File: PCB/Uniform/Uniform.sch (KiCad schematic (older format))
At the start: 158 parts, among them J2 M50-3500542, U1 STM32F373CCT6, U2 TLV1117-33, X1 XTAL_GND

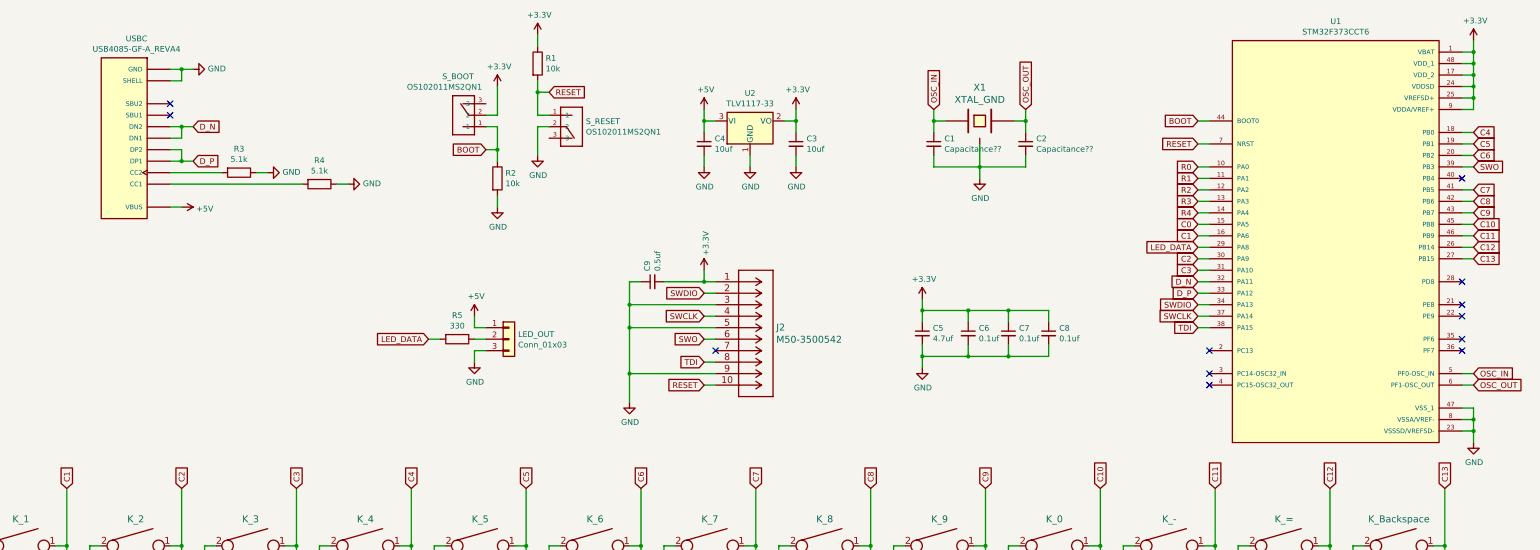
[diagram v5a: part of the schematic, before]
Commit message: Switched MCUs to STM32L072KZT6 because the F3 series went out of stock..
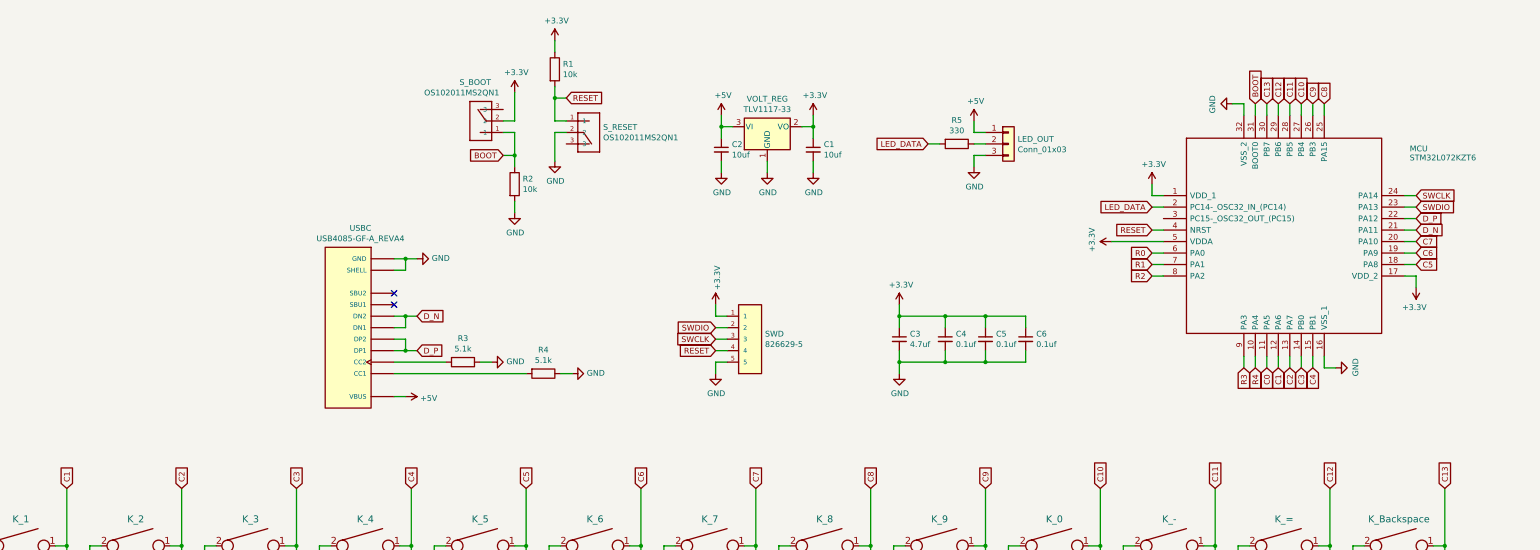
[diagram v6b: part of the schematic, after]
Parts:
- removed C1, C2: Capacitance??, symbol Device:C_Small
- removed C9: 0.5uf, symbol Device:C_Small
- removed J2: M50-3500542, CONN10_500542_HRW, symbol ul_M50-3500542:M50-3500542
- removed U1: STM32F373CCT6, QFP50P900X900X160-48N, symbol STM32F373CCT6:STM32F373CCT6
- removed X1: XTAL_GND, symbol keyboard_parts:XTAL_GND
- added MCU: STM32L072KZT6, QFP80P900X900X160-32N, symbol SamacSys_Parts:STM32L072KZT6
- added SWD: 826629-5, TE_826629-5, symbol 826629-5:826629-5
- renumbered C3 to C1, C4 to C2, C5 to C3, C6 to C4, C7 to C5, C8 to C6, U2 to VOLT_REG
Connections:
- net +3V3: now also MCU.1 (VDD_1), MCU.17 (VDD_2), MCU.5 (VDDA), SWD.1
- net BOOT: now also MCU.31 (BOOT0)
- net C0: now also MCU.11 (PA5)
- net C1: now also MCU.12 (PA6)
- net C10: now also MCU.27 (PB4)
- net C11: now also MCU.28 (PB5)
- net C12: now also MCU.29 (PB6)
- net C13: now also MCU.30 (PB7)
- net C2: now also MCU.13 (PA7)
- net C3: now also MCU.14 (PB0)
- net C4: now also MCU.15 (PB1)
- net C5: now also MCU.18 (PA8)
- net C6: now also MCU.19 (PA9)
- net C7: now also MCU.20 (PA10)
- net C8: now also MCU.25 (PA15)
- net C9: now also MCU.26 (PB3)
- net D_N: now also MCU.21 (PA11)
- net D_P: now also MCU.22 (PA12)
- net GND: now also MCU.16 (VSS_1), MCU.32 (VSS_2), SWD.5
- net LED_DATA: now also MCU.2 (PC14-_OSC32_IN_(PC14))
- net R0: now also MCU.6 (PA0)
- net R1: now also MCU.7 (PA1)
- net R2: now also MCU.8 (PA2)
- net R3: now also MCU.9 (PA3)
- net R4: now also MCU.10 (PA4)
- net RESET: now also MCU.4 (NRST), SWD.4
- net SWCLK: now also MCU.24 (PA14), SWD.3
- net SWDIO: now also MCU.23 (PA13), SWD.2
- no-connect marks 12 -> 2
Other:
- moved on the sheet: C1, C2, C3, C4, C5, C6, LED_OUT, R1, R2, R3, R4, R5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

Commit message: Schematic complete
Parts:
- removed C3: 4.7uf, symbol Device:C_Small
- removed MCU: STM32L072KZT6, QFP80P900X900X160-32N, symbol SamacSys_Parts:STM32L072KZT6
- added C6: 1uf, symbol Device:C_Small
- added MCU: STM32L072KZT6, QFP80P900X900X160-32N, symbol STM32L072KZT6:STM32L072KZT6
- added POWER_LED: LED, symbol Device:LED
- added R6: R, symbol Device:R
- renumbered C4 to C3, C6 to C4
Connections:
- net +3V3: now also C6.1, MCU.1 (VDD_1), MCU.17 (VDD_2), MCU.5 (VDDA)
- net BOOT: now also MCU.31 (BOOT0)
- net C0: now also MCU.11 (PA5)
- net C1: now also MCU.12 (PA6)
- net C10: now also MCU.27 (PB4)
- net C11: now also MCU.28 (PB5)
- net C12: now also MCU.29 (PB6)
- net C13: now also MCU.30 (PB7)
- net C2: now also MCU.13 (PA7)
- net C3: now also MCU.14 (PB0)
- net C4: now also MCU.15 (PB1)
- net C5: now also MCU.18 (PA8)
- net C6: now also MCU.19 (PA9)
- net C7: now also MCU.20 (PA10)
- net C8: now also MCU.25 (PA15)
- net C9: now also MCU.26 (PB3)
- net D_N: now also MCU.21 (PA11)
- net D_P: now also MCU.22 (PA12)
- net GND: now also C6.2, MCU.16 (VSS_1), MCU.32 (VSS_2), POWER_LED.1 (K)
- net LED_DATA: now also MCU.2 (PC14-_OSC32_IN_(PC14))
- net R0: now also MCU.6 (PA0)
- net R1: now also MCU.7 (PA1)
- net R2: now also MCU.8 (PA2)
- net R3: now also MCU.9 (PA3)
- net R4: now also MCU.10 (PA4)
- net RESET: now also MCU.4 (NRST)
- net SWCLK: now also MCU.24 (PA14)
- net SWDIO: now also MCU.23 (PA13)
- new net: POWER_LED.2 (A), R6.2
- new net STATUS_LED_DATA: MCU.3 (PC15-_OSC32_OUT_(PC15)), R6.1
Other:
- moved on the sheet: C3, C4, LED_OUT, R3, R4, R5, SWD, USBC

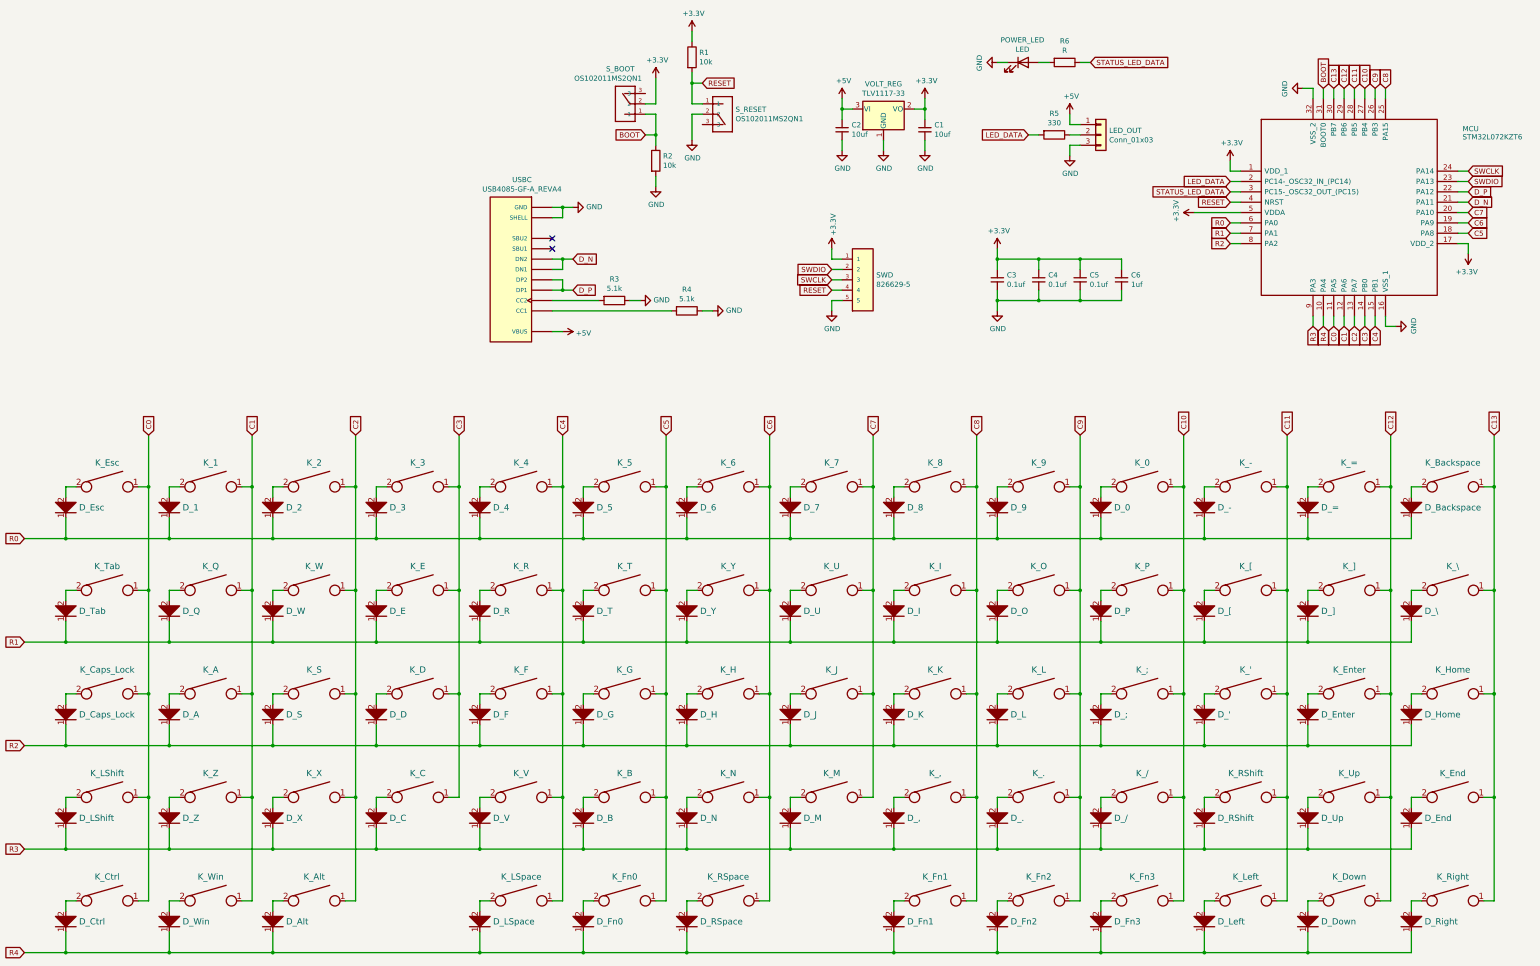
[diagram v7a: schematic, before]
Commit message: switch footprints layed out on PCB
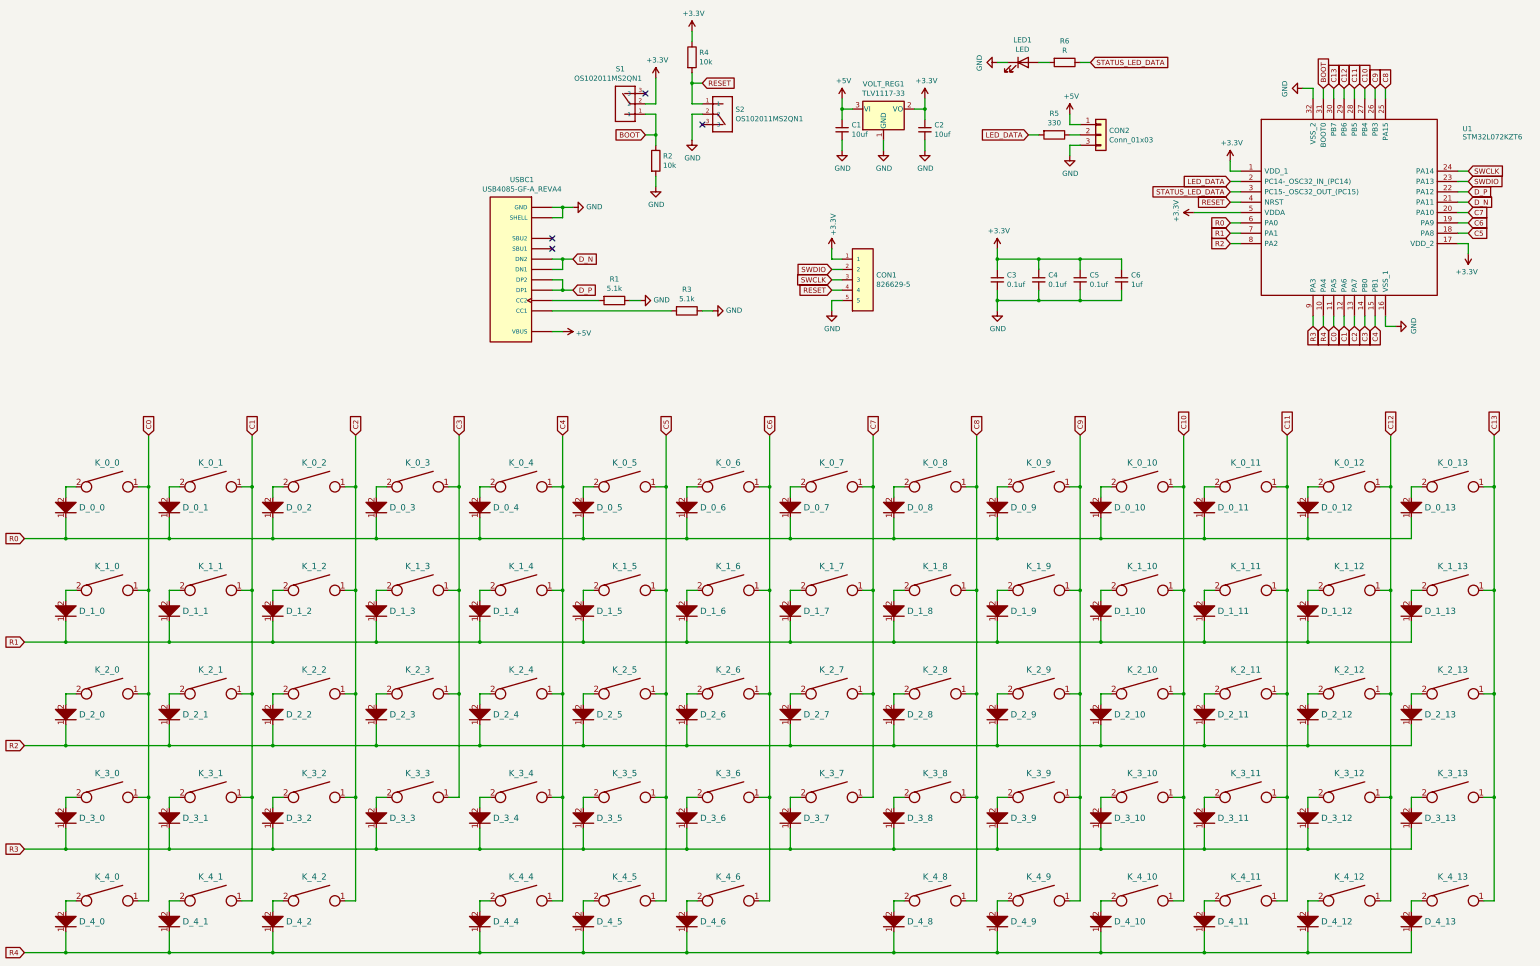
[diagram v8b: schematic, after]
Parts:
- C1: renamed from C2; footprint (none) -> ul_FG16X7R1E106KRT06:FG16X7R1E106KRT06
- C2: renamed from C1; footprint (none) -> ul_FG16X7R1E106KRT06:FG16X7R1E106KRT06
- C3, C4, C5: footprint (none) -> Resistor_THT:R_Axial_DIN0207_L6.3mm_D2.5mm_P7.62mm_Horizontal
- C6: footprint (none) -> RDER71H105K2M1H03A:CAP_RDER71H105K2M1H03A
- CON1: renamed from SWD; footprint TE_826629-5 -> 826629-5:TE_826629-5
- CON2: renamed from LED_OUT; footprint (none) -> Connector_PinHeader_2.54mm:PinHeader_1x03_P2.54mm_Vertical
- D_0_0: renamed from D_Esc; footprint (none) -> 1N4148:DIOAD829W49L456D191
- D_0_1: renamed from D_1; footprint (none) -> 1N4148:DIOAD829W49L456D191
- D_0_10: renamed from D_0; footprint (none) -> 1N4148:DIOAD829W49L456D191
- D_0_11: renamed from D_-; footprint (none) -> 1N4148:DIOAD829W49L456D191
- D_0_12: renamed from D_=; footprint (none) -> 1N4148:DIOAD829W49L456D191
- D_0_13: renamed from D_Backspace; footprint (none) -> 1N4148:DIOAD829W49L456D191
- D_0_2: renamed from D_2; footprint (none) -> 1N4148:DIOAD829W49L456D191
- D_0_3: renamed from D_3; footprint (none) -> 1N4148:DIOAD829W49L456D191
- D_0_4: renamed from D_4; footprint (none) -> 1N4148:DIOAD829W49L456D191
- D_0_5: renamed from D_5; footprint (none) -> 1N4148:DIOAD829W49L456D191
- D_0_6: renamed from D_6; footprint (none) -> 1N4148:DIOAD829W49L456D191
- D_0_7: renamed from D_7; footprint (none) -> 1N4148:DIOAD829W49L456D191
- D_0_8: renamed from D_8; footprint (none) -> 1N4148:DIOAD829W49L456D191
- D_0_9: renamed from D_9; footprint (none) -> 1N4148:DIOAD829W49L456D191
- D_1_0: renamed from D_Tab; footprint (none) -> 1N4148:DIOAD829W49L456D191
- D_1_1: renamed from D_Q; footprint (none) -> 1N4148:DIOAD829W49L456D191
- D_1_10: renamed from D_P; footprint (none) -> 1N4148:DIOAD829W49L456D191
- D_1_11: renamed from D_[; footprint (none) -> 1N4148:DIOAD829W49L456D191
- D_1_12: renamed from D_]; footprint (none) -> 1N4148:DIOAD829W49L456D191
- D_1_13: renamed from D_\; footprint (none) -> 1N4148:DIOAD829W49L456D191
- D_1_2: renamed from D_W; footprint (none) -> 1N4148:DIOAD829W49L456D191
- D_1_3: renamed from D_E; footprint (none) -> 1N4148:DIOAD829W49L456D191
- D_1_4: renamed from D_R; footprint (none) -> 1N4148:DIOAD829W49L456D191
- D_1_5: renamed from D_T; footprint (none) -> 1N4148:DIOAD829W49L456D191
- D_1_6: renamed from D_Y; footprint (none) -> 1N4148:DIOAD829W49L456D191
- D_1_7: renamed from D_U; footprint (none) -> 1N4148:DIOAD829W49L456D191
- D_1_8: renamed from D_I; footprint (none) -> 1N4148:DIOAD829W49L456D191
- D_1_9: renamed from D_O; footprint (none) -> 1N4148:DIOAD829W49L456D191
- D_2_0: renamed from D_Caps_Lock; footprint (none) -> 1N4148:DIOAD829W49L456D191
- D_2_1: renamed from D_A; footprint (none) -> 1N4148:DIOAD829W49L456D191
- D_2_10: renamed from D_;; footprint (none) -> 1N4148:DIOAD829W49L456D191
- D_2_11: renamed from D_'; footprint (none) -> 1N4148:DIOAD829W49L456D191
- D_2_12: renamed from D_Enter; footprint (none) -> 1N4148:DIOAD829W49L456D191
- D_2_13: renamed from D_Home; footprint (none) -> 1N4148:DIOAD829W49L456D191
- D_2_2: renamed from D_S; footprint (none) -> 1N4148:DIOAD829W49L456D191
- D_2_3: renamed from D_D; footprint (none) -> 1N4148:DIOAD829W49L456D191
- D_2_4: renamed from D_F; footprint (none) -> 1N4148:DIOAD829W49L456D191
- D_2_5: renamed from D_G; footprint (none) -> 1N4148:DIOAD829W49L456D191
- D_2_6: renamed from D_H; footprint (none) -> 1N4148:DIOAD829W49L456D191
- D_2_7: renamed from D_J; footprint (none) -> 1N4148:DIOAD829W49L456D191
- D_2_8: renamed from D_K; footprint (none) -> 1N4148:DIOAD829W49L456D191
- D_2_9: renamed from D_L; footprint (none) -> 1N4148:DIOAD829W49L456D191
- D_3_0: renamed from D_LShift; footprint (none) -> 1N4148:DIOAD829W49L456D191
- D_3_1: renamed from D_Z; footprint (none) -> 1N4148:DIOAD829W49L456D191
- D_3_10: renamed from D_/; footprint (none) -> 1N4148:DIOAD829W49L456D191
- D_3_11: renamed from D_RShift; footprint (none) -> 1N4148:DIOAD829W49L456D191
- D_3_12: renamed from D_Up; footprint (none) -> 1N4148:DIOAD829W49L456D191
- D_3_13: renamed from D_End; footprint (none) -> 1N4148:DIOAD829W49L456D191
- D_3_2: renamed from D_X; footprint (none) -> 1N4148:DIOAD829W49L456D191
- D_3_3: renamed from D_C; footprint (none) -> 1N4148:DIOAD829W49L456D191
- D_3_4: renamed from D_V; footprint (none) -> 1N4148:DIOAD829W49L456D191
- D_3_5: renamed from D_B; footprint (none) -> 1N4148:DIOAD829W49L456D191
- D_3_6: renamed from D_N; footprint (none) -> 1N4148:DIOAD829W49L456D191
- D_3_7: renamed from D_M; footprint (none) -> 1N4148:DIOAD829W49L456D191
- D_3_8: renamed from D_,; footprint (none) -> 1N4148:DIOAD829W49L456D191
- D_3_9: renamed from D_.; footprint (none) -> 1N4148:DIOAD829W49L456D191
- D_4_0: renamed from D_Ctrl; footprint (none) -> 1N4148:DIOAD829W49L456D191
- D_4_1: renamed from D_Win; footprint (none) -> 1N4148:DIOAD829W49L456D191
- D_4_10: renamed from D_Fn3; footprint (none) -> 1N4148:DIOAD829W49L456D191
- D_4_11: renamed from D_Left; footprint (none) -> 1N4148:DIOAD829W49L456D191
- D_4_12: renamed from D_Down; footprint (none) -> 1N4148:DIOAD829W49L456D191
- D_4_13: renamed from D_Right; footprint (none) -> 1N4148:DIOAD829W49L456D191
- D_4_2: renamed from D_Alt; footprint (none) -> 1N4148:DIOAD829W49L456D191
- D_4_4: renamed from D_LSpace; footprint (none) -> 1N4148:DIOAD829W49L456D191
- D_4_5: renamed from D_Fn0; footprint (none) -> 1N4148:DIOAD829W49L456D191
- D_4_6: renamed from D_RSpace; footprint (none) -> 1N4148:DIOAD829W49L456D191
- D_4_8: renamed from D_Fn1; footprint (none) -> 1N4148:DIOAD829W49L456D191
- D_4_9: renamed from D_Fn2; footprint (none) -> 1N4148:DIOAD829W49L456D191
- K_0_0: renamed from K_Esc; footprint (none) -> keyswitches:SW_MX
- K_0_1: renamed from K_1; footprint (none) -> keyswitches:SW_MX
- K_0_10: renamed from K_0; footprint (none) -> keyswitches:SW_MX
- K_0_11: renamed from K_-; footprint (none) -> keyswitches:SW_MX
- K_0_12: renamed from K_=; footprint (none) -> keyswitches:SW_MX
- K_0_13: renamed from K_Backspace; footprint (none) -> keyswitches:SW_MX
- K_0_2: renamed from K_2; footprint (none) -> keyswitches:SW_MX
- K_0_3: renamed from K_3; footprint (none) -> keyswitches:SW_MX
- K_0_4: renamed from K_4; footprint (none) -> keyswitches:SW_MX
- K_0_5: renamed from K_5; footprint (none) -> keyswitches:SW_MX
- K_0_6: renamed from K_6; footprint (none) -> keyswitches:SW_MX
- K_0_7: renamed from K_7; footprint (none) -> keyswitches:SW_MX
- K_0_8: renamed from K_8; footprint (none) -> keyswitches:SW_MX
- K_0_9: renamed from K_9; footprint (none) -> keyswitches:SW_MX
- K_1_0: renamed from K_Tab; footprint (none) -> keyswitches:SW_MX
- K_1_1: renamed from K_Q; footprint (none) -> keyswitches:SW_MX
- K_1_10: renamed from K_P; footprint (none) -> keyswitches:SW_MX
- K_1_11: renamed from K_[; footprint (none) -> keyswitches:SW_MX
- K_1_12: renamed from K_]; footprint (none) -> keyswitches:SW_MX
- K_1_13: renamed from K_\; footprint (none) -> keyswitches:SW_MX
- K_1_2: renamed from K_W; footprint (none) -> keyswitches:SW_MX
- K_1_3: renamed from K_E; footprint (none) -> keyswitches:SW_MX
- K_1_4: renamed from K_R; footprint (none) -> keyswitches:SW_MX
- K_1_5: renamed from K_T; footprint (none) -> keyswitches:SW_MX
- K_1_6: renamed from K_Y; footprint (none) -> keyswitches:SW_MX
- K_1_7: renamed from K_U; footprint (none) -> keyswitches:SW_MX
- K_1_8: renamed from K_I; footprint (none) -> keyswitches:SW_MX
- K_1_9: renamed from K_O; footprint (none) -> keyswitches:SW_MX
- K_2_0: renamed from K_Caps_Lock; footprint (none) -> keyswitches:SW_MX
- K_2_1: renamed from K_A; footprint (none) -> keyswitches:SW_MX
- K_2_10: renamed from K_;; footprint (none) -> keyswitches:SW_MX
- K_2_11: renamed from K_'; footprint (none) -> keyswitches:SW_MX
- K_2_12: renamed from K_Enter; footprint (none) -> keyswitches:SW_MX
- K_2_13: renamed from K_Home; footprint (none) -> keyswitches:SW_MX
- K_2_2: renamed from K_S; footprint (none) -> keyswitches:SW_MX
- K_2_3: renamed from K_D; footprint (none) -> keyswitches:SW_MX
- K_2_4: renamed from K_F; footprint (none) -> keyswitches:SW_MX
- K_2_5: renamed from K_G; footprint (none) -> keyswitches:SW_MX
- K_2_6: renamed from K_H; footprint (none) -> keyswitches:SW_MX
- K_2_7: renamed from K_J; footprint (none) -> keyswitches:SW_MX
- K_2_8: renamed from K_K; footprint (none) -> keyswitches:SW_MX
- K_2_9: renamed from K_L; footprint (none) -> keyswitches:SW_MX
- K_3_0: renamed from K_LShift; footprint (none) -> keyswitches:SW_MX
- K_3_1: renamed from K_Z; footprint (none) -> keyswitches:SW_MX
- K_3_10: renamed from K_/; footprint (none) -> keyswitches:SW_MX
- K_3_11: renamed from K_RShift; footprint (none) -> keyswitches:SW_MX
- K_3_12: renamed from K_Up; footprint (none) -> keyswitches:SW_MX
- K_3_13: renamed from K_End; footprint (none) -> keyswitches:SW_MX
- K_3_2: renamed from K_X; footprint (none) -> keyswitches:SW_MX
- K_3_3: renamed from K_C; footprint (none) -> keyswitches:SW_MX
- K_3_4: renamed from K_V; footprint (none) -> keyswitches:SW_MX
- K_3_5: renamed from K_B; footprint (none) -> keyswitches:SW_MX
- K_3_6: renamed from K_N; footprint (none) -> keyswitches:SW_MX
- K_3_7: renamed from K_M; footprint (none) -> keyswitches:SW_MX
- K_3_8: renamed from K_,; footprint (none) -> keyswitches:SW_MX
- K_3_9: renamed from K_.; footprint (none) -> keyswitches:SW_MX
- K_4_0: renamed from K_Ctrl; footprint (none) -> keyswitches:SW_MX
- K_4_1: renamed from K_Win; footprint (none) -> keyswitches:SW_MX
- K_4_10: renamed from K_Fn3; footprint (none) -> keyswitches:SW_MX
- K_4_11: renamed from K_Left; footprint (none) -> keyswitches:SW_MX
- K_4_12: renamed from K_Down; footprint (none) -> keyswitches:SW_MX
- K_4_13: renamed from K_Right; footprint (none) -> keyswitches:SW_MX
- K_4_2: renamed from K_Alt; footprint (none) -> keyswitches:SW_MX
- K_4_4: renamed from K_LSpace; footprint (none) -> keyswitches:SW_MX
- K_4_5: renamed from K_Fn0; footprint (none) -> keyswitches:SW_MX
- K_4_6: renamed from K_RSpace; footprint (none) -> keyswitches:SW_MX
- K_4_8: renamed from K_Fn1; footprint (none) -> keyswitches:SW_MX
- K_4_9: renamed from K_Fn2; footprint (none) -> keyswitches:SW_MX
- LED1: renamed from POWER_LED; footprint (none) -> LED_THT:LED_D5.0mm_Clear
- R1: renamed from R3; footprint (none) -> Resistor_THT:R_Axial_DIN0309_L9.0mm_D3.2mm_P12.70mm_Horizontal
- R2, R5, R6: footprint (none) -> Resistor_THT:R_Axial_DIN0309_L9.0mm_D3.2mm_P12.70mm_Horizontal
- R3: renamed from R4; footprint (none) -> Resistor_THT:R_Axial_DIN0309_L9.0mm_D3.2mm_P12.70mm_Horizontal
- R4: renamed from R1; footprint (none) -> Resistor_THT:R_Axial_DIN0309_L9.0mm_D3.2mm_P12.70mm_Horizontal
- S1: renamed from S_BOOT; footprint SW_OS102011MS2QN1 -> OS102011MS2QN1:SW_OS102011MS2QN1
- S2: renamed from S_RESET; footprint SW_OS102011MS2QN1 -> OS102011MS2QN1:SW_OS102011MS2QN1
- U1: renamed from MCU; footprint QFP80P900X900X160-32N -> STM32L072KZT6:QFP80P900X900X160-32N
- USBC1: renamed from USBC; footprint GCT_USB4085-GF-A_REVA4 -> USB4085-GF-A_REVA4:GCT_USB4085-GF-A_REVA4
- VOLT_REG1: renamed from VOLT_REG; footprint (none) -> TLV1117-33IDCY:SOT230P700X180-4N
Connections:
- no-connect marks 2 -> 4
